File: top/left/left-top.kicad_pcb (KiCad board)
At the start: 2 copper layers, 137.8 x 95 mm, 30 parts

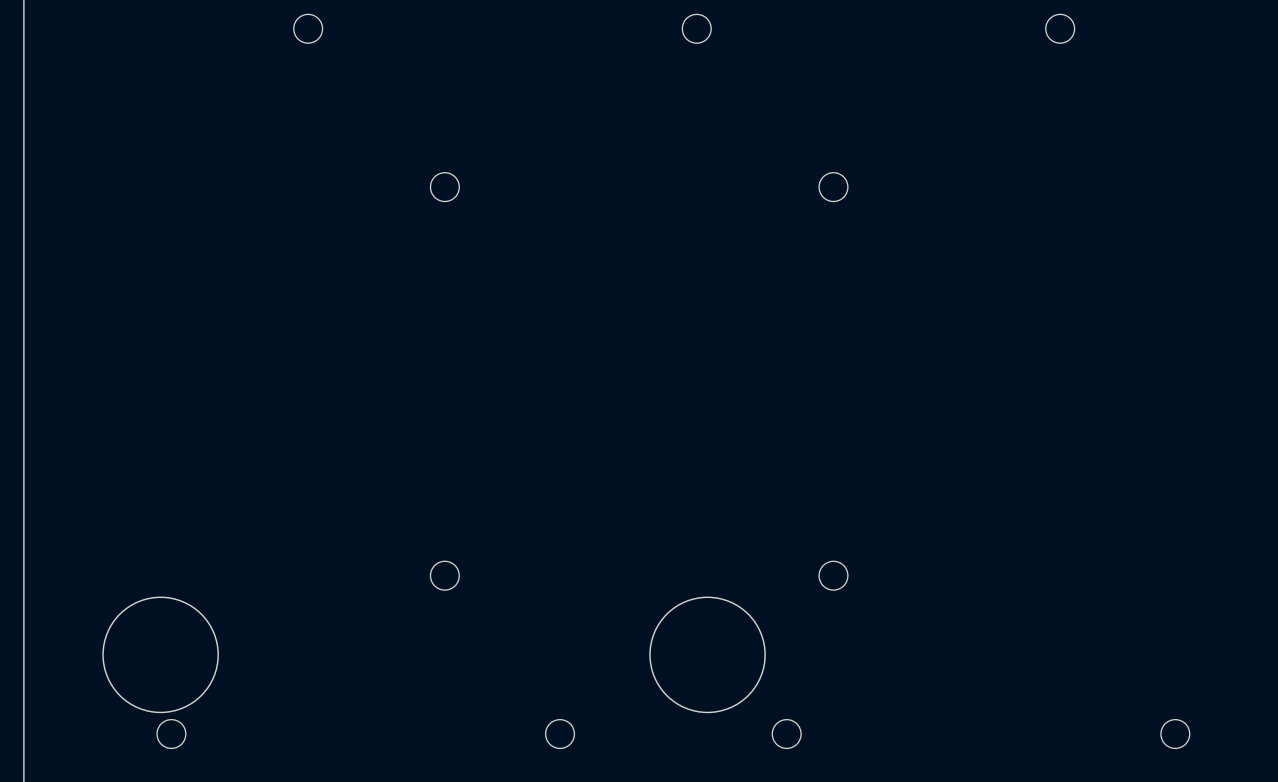
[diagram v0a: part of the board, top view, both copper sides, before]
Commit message: change stabilizer cutout
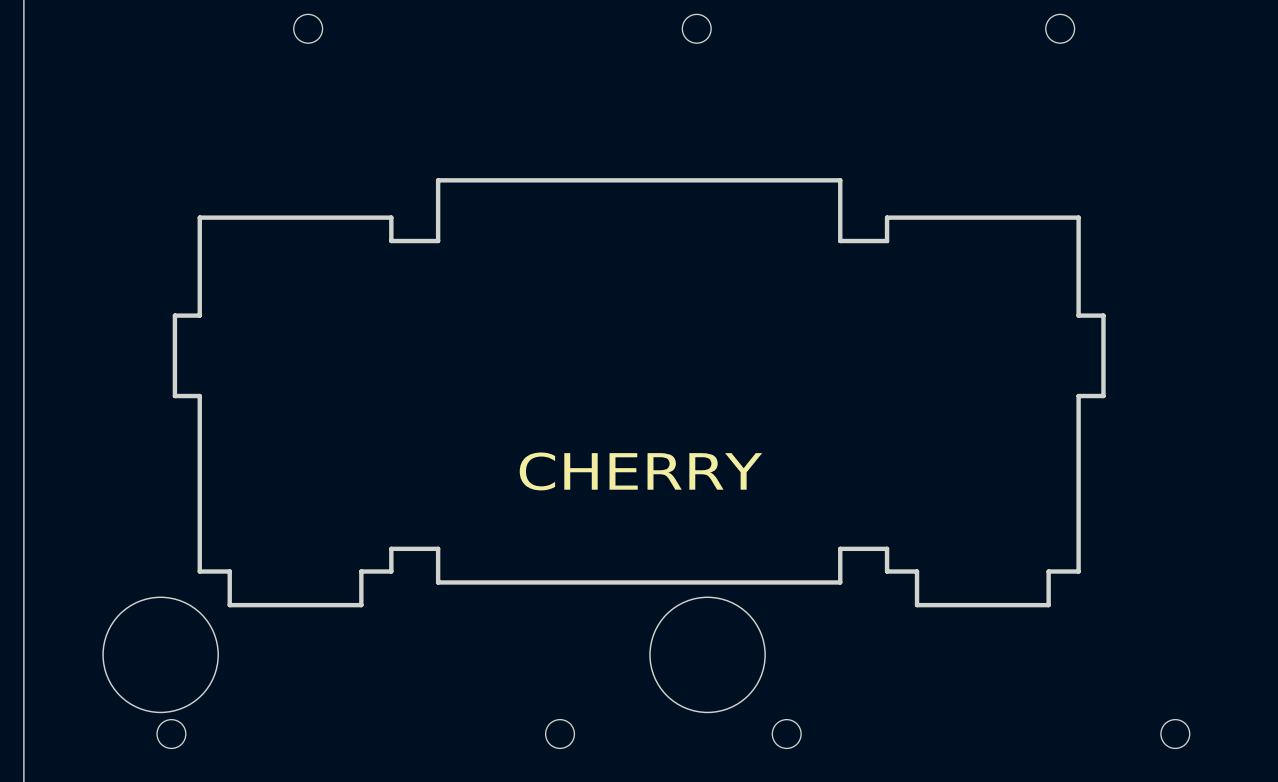
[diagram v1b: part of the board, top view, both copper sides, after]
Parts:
- removed the MX_CUTOUT at (102.1, 123.5)
- removed the REF** at (102.1, 123.5)
- added CHERRY: MX, lib:MX_PCB_CUTOUT, F.Cu at (102.1, 123.5)
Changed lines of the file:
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@@
     (tracks 0)
     (zones 0)
-    (modules 30)
+    (modules 29)
     (nets 1)
   )
@@
     (uvia_dia 0.3)
     (uvia_drill 0.1)
+  )
+  (module lib:MX_PCB_CUTOUT (layer F.Cu)
+    (at 102.125 123.5)
+    (fp_text reference CHERRY (at 0 3.175) (layer F.SilkS)
+      (effects (font (size 1.27 1.524) (thickness 0.2032)))
+    )
+    (fp_text value MX (at 0 5.08) (layer F.SilkS) hide
+      (effects (font (size 1.27 1.524) (thickness 0.2032)))
+    )
+    (fp_circle (center 11.938 8.255) (end 13.938 8.255) (layer Dwgs.User) (width 0.12))
+    (fp_circle (center -11.938 8.255) (end -9.938 8.255) (layer Dwgs.User) (width 0.12))
+    (fp_circle (center -11.938 -6.985) (end -10.438 -6.985) (layer Dwgs.User) (width 0.12))
+    (fp_circle (center 11.938 -6.985) (end 13.438 -6.985) (layer Dwgs.User) (width 0.12))
+    (fp_circle (center 0 0) (end 2 0) (layer Dwgs.User) (width 0.12))
+    (fp_line (start -6.985 -6.985) (end 6.985 -6.985) (layer Edge.Cuts) (width 0.1524))
+    (fp_line (start 6.985 -6.985) (end 6.985 -4.8768) (layer Edge.Cuts) (width 0.1524))
+    (fp_line (start 6.985 -4.8768) (end 8.6106 -4.8768) (layer Edge.Cuts) (width 0.1524))
+    (fp_line (start 8.6106 -4.8768) (end 8.6106 -5.6896) (layer Edge.Cuts) (width 0.1524))
+    (fp_line (start 8.6106 -5.6896) (end 15.2654 -5.6896) (layer Edge.Cuts) (width 0.1524))
+    (fp_line (start 15.2654 -5.6896) (end 15.2654 -2.286) (layer Edge.Cuts) (width 0.1524))
+    (fp_line (start 15.2654 -2.286) (end 16.129 -2.286) (layer Edge.Cuts) (width 0.1524))
+    (fp_line (start 16.129 -2.286) (end 16.129 0.508) (layer Edge.Cuts) (width 0.1524))
+    (fp_line (start 16.129 0.508) (end 15.2654 0.508) (layer Edge.Cuts) (width 0.1524))
+    (fp_line (start 15.2654 0.508) (end 15.2654 6.604) (layer Edge.Cuts) (width 0.1524))
+    (fp_line (start 15.2654 6.604) (end 14.224 6.604) (layer Edge.Cuts) (width 0.1524))
+    (fp_line (start 14.224 6.604) (end 14.224 7.7724) (layer Edge.Cuts) (width 0.1524))
+    (fp_line (start 14.224 7.7724) (end 9.652 7.7724) (layer Edge.Cuts) (width 0.1524))
+    (fp_line (start 9.652 7.7724) (end 9.652 6.604) (layer Edge.Cuts) (width 0.1524))
+    (fp_line (start 9.652 6.604) (end 8.6106 6.604) (layer Edge.Cuts) (width 0.1524))
+    (fp_line (start 8.6106 6.604) (end 8.6106 5.8166) (layer Edge.Cuts) (width 0.1524))
+    (fp_line (start 8.6106 5.8166) (end 6.985 5.8166) (layer Edge.Cuts) (width 0.1524))
+    (fp_line (start 6.985 5.8166) (end 6.985 6.985) (layer Edge.Cuts) (width 0.1524))
+    (fp_line (start 6.985 6.985) (end -6.985 6.985) (layer Edge.Cuts) (width 0.1524))
+    (fp_line (start -6.985 6.985) (end -6.985 5.8166) (layer Edge.Cuts) (width 0.1524))
+    (fp_line (start -6.985 5.8166) (end -8.6106 5.8166) (layer Edge.Cuts) (width 0.1524))
+    (fp_line (start -8.6106 5.8166) (end -8.6106 6.604) (layer Edge.Cuts) (width 0.1524))
+    (fp_line (start -8.6106 6.604) (end -9.652 6.604) (layer Edge.Cuts) (width 0.1524))
+    (fp_line (start -9.652 6.604) (end -9.652 7.7724) (layer Edge.Cuts) (width 0.1524))
+    (fp_line (start -9.652 7.7724) (end -14.224 7.7724) (layer Edge.Cuts) (width 0.1524))
+    (fp_line (start -14.224 7.7724) (end -14.224 6.604) (layer Edge.Cuts) (width 0.1524))
+    (fp_line (start -14.224 6.604) (end -15.2654 6.604) (layer Edge.Cuts) (width 0.1524))
+    (fp_line (start -15.2654 6.604) (end -15.2654 0.508) (layer Edge.Cuts) (width 0.1524))
+    (fp_line (start -15.2654 0.508) (end -16.129 0.508) (layer Edge.Cuts) (width 0.1524))
+    (fp_line (start -16.129 0.508) (end -16.129 -2.286) (layer Edge.Cuts) (width 0.1524))
+    (fp_line (start -16.129 -2.286) (end -15.2654 -2.286) (layer Edge.Cuts) (width 0.1524))
+    (fp_line (start -15.2654 -2.286) (end -15.2654 -5.6896) (layer Edge.Cuts) (width 0.1524))
+    (fp_line (start -15.2654 -5.6896) (end -8.6106 -5.6896) (layer Edge.Cuts) (width 0.1524))
+    (fp_line (start -8.6106 -5.6896) (end -8.6106 -4.8768) (layer Edge.Cuts) (width 0.1524))
+    (fp_line (start -8.6106 -4.8768) (end -6.985 -4.8768) (layer Edge.Cuts) (width 0.1524))
+    (fp_line (start -6.985 -4.8768) (end -6.985 -6.985) (layer Edge.Cuts) (width 0.1524))
+    (fp_line (start 15.367 -7.62) (end 8.509 -7.62) (layer Cmts.User) (width 0.1524))
+    (fp_line (start 8.509 -7.62) (end 8.509 7.62) (layer Cmts.User) (width 0.1524))
+    (fp_line (start 8.509 7.62) (end -8.509 7.62) (layer Cmts.User) (width 0.1524))
+    (fp_line (start -8.509 7.62) (end -8.509 -7.62) (layer Cmts.User) (width 0.1524))
+    (fp_line (start -8.509 -7.62) (end -15.367 -7.62) (layer Cmts.User) (width 0.1524))
+    (fp_line (start -15.367 -7.62) (end -15.367 10.16) (layer Cmts.User) (width 0.1524))
+    (fp_line (start -15.367 10.16) (end 15.367 10.16) (layer Cmts.User) (width 0.1524))
+    (fp_line (start 15.367 10.16) (end 15.367 -7.62) (layer Cmts.User) (width 0.1524))
   )
   (module lib:MX_CUTOFF_BackSpace (layer F.Cu)
@@
     (pad "" np_thru_hole circle (at -6.75 -6.75) (size 1 1) (drill 1) (layers *.Cu *.Mask))
   )
-  (module lib:MX_CUTOUT_min_dril_1mm (layer F.Cu)
-    (at 102.125 123.5)
-    (fp_text reference MX_CUTOUT (at 0 1.5) (layer F.SilkS) hide
-      (effects (font (size 1 1) (thickness 0.15)))
-    )
-    (fp_text value VAL** (at 0 0) (layer F.SilkS) hide
-      (effects (font (size 1 1) (thickness 0.15)))
-    )
-    (fp_line (start -7 7) (end -7 -7) (layer Dwgs.User) (width 0.12))
-    (fp_line (start 7 7) (end -7 7) (layer Dwgs.User) (width 0.12))
-    (fp_line (start 7 -7) (end 7 7) (layer Dwgs.User) (width 0.12))
-    (fp_line (start -7 -7) (end 7 -7) (layer Dwgs.User) (width 0.12))
-    (pad "" np_thru_hole oval (at 6.5 0 90) (size 14 1) (drill oval 14 1) (layers *.Cu *.Mask))
-    (pad "" np_thru_hole oval (at -6.5 0 90) (size 14 1) (drill oval 14 1) (layers *.Cu *.Mask))
-    (pad "" np_thru_hole oval (at 0 6.5) (size 14 1) (drill oval 14 1) (layers *.Cu *.Mask))
-    (pad "" np_thru_hole oval (at 0 -6.5) (size 14 1) (drill oval 14 1) (layers *.Cu *.Mask))
-    (pad "" np_thru_hole circle (at -6.75 6.75) (size 1 1) (drill 1) (layers *.Cu *.Mask))
-    (pad "" np_thru_hole circle (at 6.75 6.75) (size 1 1) (drill 1) (layers *.Cu *.Mask))
-    (pad "" np_thru_hole circle (at 6.75 -6.75) (size 1 1) (drill 1) (layers *.Cu *.Mask))
-    (pad "" np_thru_hole circle (at -6.75 -6.75) (size 1 1) (drill 1) (layers *.Cu *.Mask))
-  )
-  (module Keebio-Parts:MX_Stabilizer_Cutout-2u (layer F.Cu)
-    (at 102.125 123.5)
-    (fp_text reference REF** (at 0.25 10.05) (layer Eco2.User) hide
-      (effects (font (size 1 1) (thickness 0.15)))
-    )
-    (fp_text value MX_Stabilizer_Cutout-2u (at 0 -15.24) (layer F.Fab) hide
-      (effects (font (size 1 1) (thickness 0.15)))
-    )
-    (fp_line (start 19 -9.5) (end 19 9.5) (layer Dwgs.User) (width 0.15))
-    (fp_line (start 19 9.5) (end -19 9.5) (layer Dwgs.User) (width 0.15))
-    (fp_line (start -19 9.5) (end -19 -9.5) (layer Dwgs.User) (width 0.15))
-    (fp_line (start -19 -9.5) (end 19 -9.5) (layer Dwgs.User) (width 0.15))
-    (pad "" np_thru_hole oval (at -11.938 7.7724) (size 3.048 0.3048) (drill oval 3.048 0.3048) (layers *.Cu *.Mask))
-    (pad "" np_thru_hole oval (at -10.5664 7.112) (size 0.3048 1.4732) (drill oval 0.3048 1.4732) (layers *.Cu *.Mask))
-    (pad "" np_thru_hole oval (at -13.3096 7.112) (size 0.3048 1.4732) (drill oval 0.3048 1.4732) (layers *.Cu *.Mask))
-    (pad "" np_thru_hole oval (at -15.5448 0.3556) (size 1.1684 0.3048) (drill oval 1.1684 0.3048) (layers *.Cu *.Mask))
-    (pad "" np_thru_hole oval (at -11.938 6.4516) (size 6.6548 0.3048) (drill oval 6.6548 0.3048) (layers *.Cu *.Mask))
-    (pad "" np_thru_hole oval (at -8.763 0.4572) (size 0.3048 12.2936) (drill oval 0.3048 12.2936) (layers *.Cu *.Mask))
-    (pad "" np_thru_hole oval (at -15.113 0.4572) (size 0.3048 12.2936) (drill oval 0.3048 12.2936) (layers *.Cu *.Mask))
-    (pad "" np_thru_hole oval (at -15.9766 -0.889) (size 0.3048 2.794) (drill oval 0.3048 2.794) (layers *.Cu *.Mask))
-    (pad "" np_thru_hole oval (at -15.5448 -2.1336) (size 1.1684 0.3048) (drill oval 1.1684 0.3048) (layers *.Cu *.Mask))
-    (pad "" np_thru_hole oval (at -11.938 -5.5372) (size 6.6548 0.3048) (drill oval 6.6548 0.3048) (layers *.Cu *.Mask))
-    (pad "" np_thru_hole oval (at 15.5448 0.3556) (size 1.1684 0.3048) (drill oval 1.1684 0.3048) (layers *.Cu *.Mask))
-    (pad "" np_thru_hole oval (at 13.3096 7.112) (size 0.3048 1.4732) (drill oval 0.3048 1.4732) (layers *.Cu *.Mask))
-    (pad "" np_thru_hole oval (at 15.5448 -2.1336) (size 1.1684 0.3048) (drill oval 1.1684 0.3048) (layers *.Cu *.Mask))
-    (pad "" np_thru_hole oval (at 10.5664 7.112) (size 0.3048 1.4732) (drill oval 0.3048 1.4732) (layers *.Cu *.Mask))
-    (pad "" np_thru_hole oval (at 15.9766 -0.889) (size 0.3048 2.794) (drill oval 0.3048 2.794) (layers *.Cu *.Mask))
-    (pad "" np_thru_hole oval (at 15.113 0.4572) (size 0.3048 12.2936) (drill oval 0.3048 12.2936) (layers *.Cu *.Mask))
-    (pad "" np_thru_hole oval (at 11.938 6.4516) (size 6.6548 0.3048) (drill oval 6.6548 0.3048) (layers *.Cu *.Mask))
-    (pad "" np_thru_hole oval (at 8.763 0.4572) (size 0.3048 12.2936) (drill oval 0.3048 12.2936) (layers *.Cu *.Mask))
-    (pad "" np_thru_hole oval (at 11.938 -5.5372) (size 6.6548 0.3048) (drill oval 6.6548 0.3048) (layers *.Cu *.Mask))
-    (pad "" np_thru_hole oval (at 11.938 7.7724) (size 3.048 0.3048) (drill oval 3.048 0.3048) (layers *.Cu *.Mask))
-  )
   (gr_circle (center 99.75 76) (end 101.75 76) (layer Edge.Cuts) (width 0.05))

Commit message: move screw holl
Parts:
- added REF**: MountingHole_3.7mm, MountingHole:MountingHole_3.7mm, F.Cu at (99.8, 76.0)
- added REF**: MountingHole_3.7mm, MountingHole:MountingHole_3.7mm, F.Cu at (185.2, 76.0)
- added REF**: MountingHole_3.7mm, MountingHole:MountingHole_3.7mm, F.Cu at (199.5, 114.0)
- added REF**: MountingHole_3.7mm, MountingHole:MountingHole_3.7mm, F.Cu at (185.2, 133.0)
- added REF**: MountingHole_3.7mm, MountingHole:MountingHole_3.7mm, F.Cu at (166.2, 133.0)
- added REF**: MountingHole_3.7mm, MountingHole:MountingHole_3.7mm, F.Cu at (123.5, 133.0)
- added REF**: MountingHole_3.7mm, MountingHole:MountingHole_3.7mm, F.Cu at (82.5, 132.7)
- MX_CUTOUT (x27): footprint lib:MX_CUTOUT_min_dril_1mm -> lib:MX_CUTOUT
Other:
- outline, holes or cut-outs redrawn
- board text added: "rev.1"
